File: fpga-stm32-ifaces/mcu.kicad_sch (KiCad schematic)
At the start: 58 parts, among them J10 CORTEX_DEBUG_ETM, J3 PMOD_HOST, J4 XILINX_JTAG, J5 CONN_01X03, U1 STM32H735-UFBGA176-25, U16 W25Q128JV, U2 XC7S25-1FTGB196, U8 AT24MAC402, U9 ECS-1612MV-250-CN

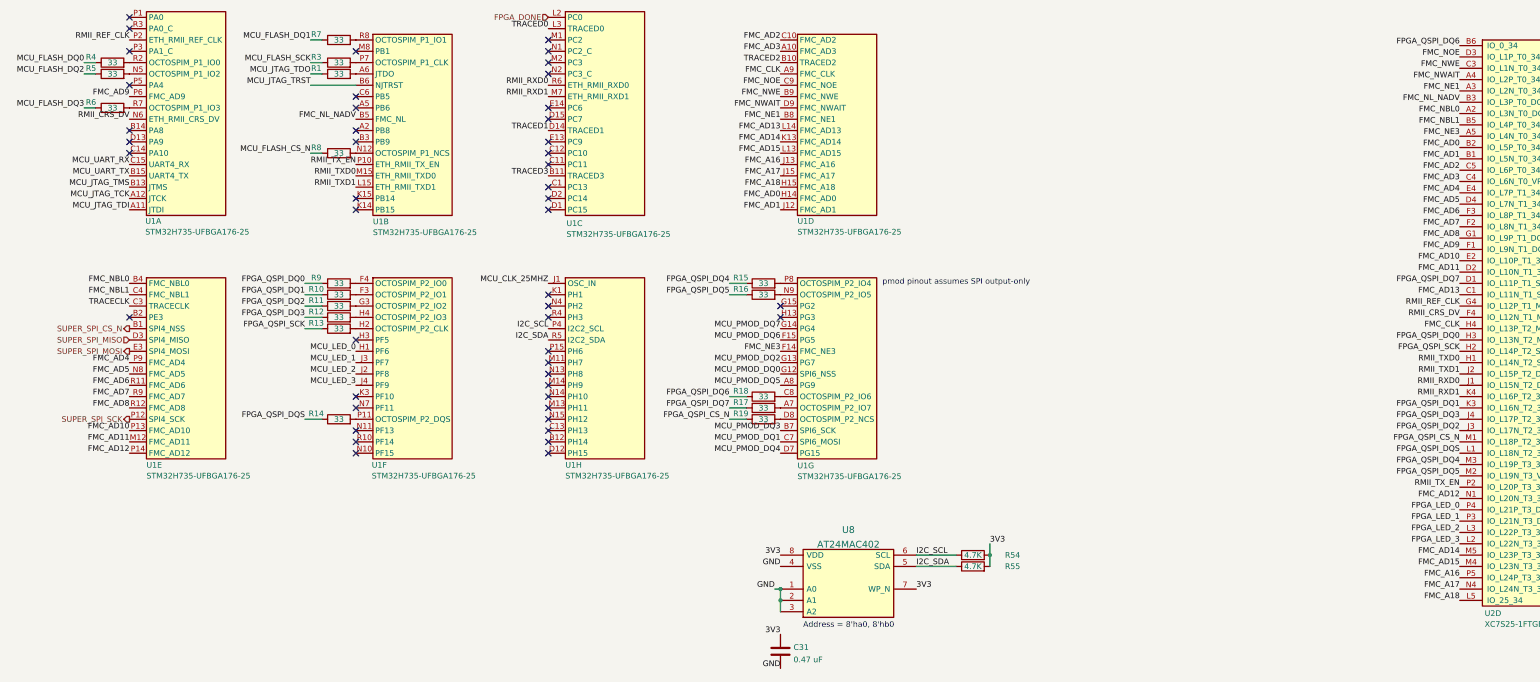
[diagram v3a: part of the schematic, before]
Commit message: Routed most FPGA decoupling caps plus most of RGMII
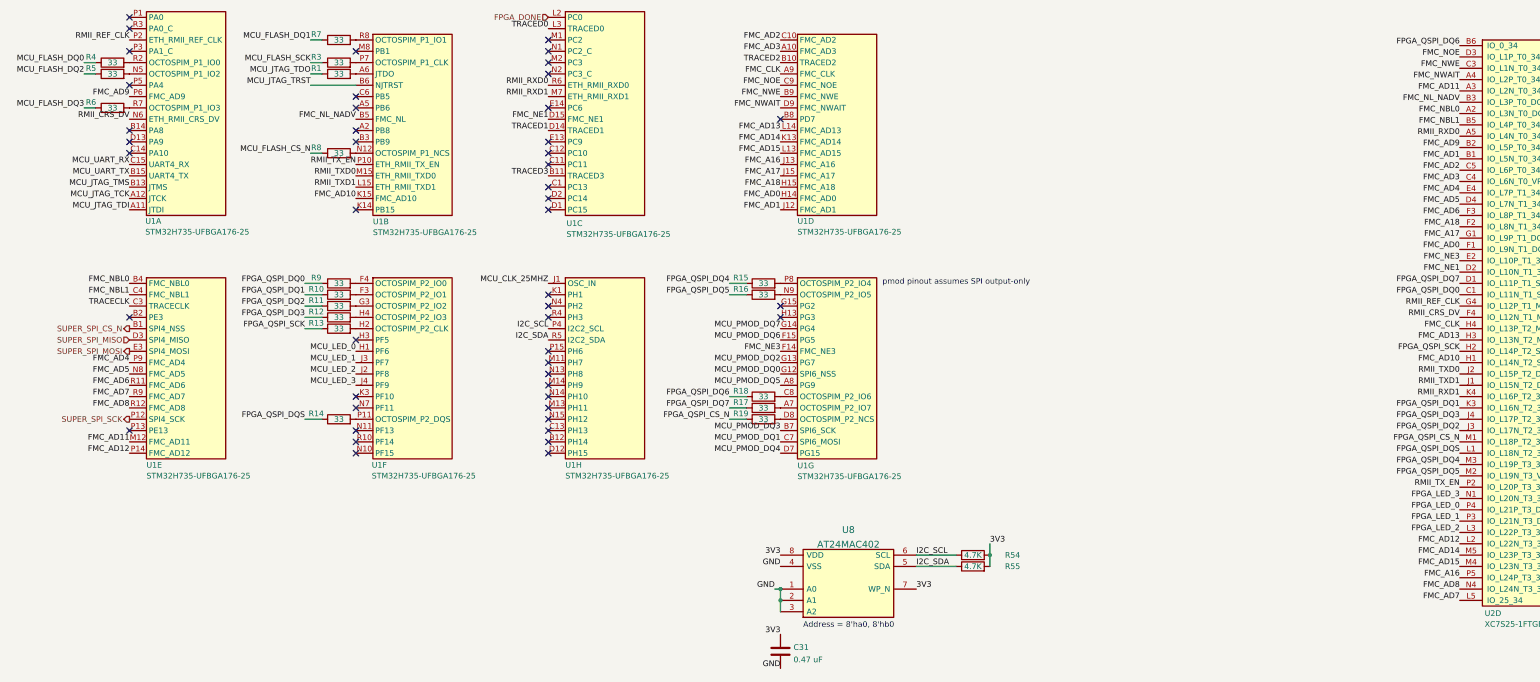
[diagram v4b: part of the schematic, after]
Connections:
- net FMC_A17: now also U2.G1 (IO_L9P_T1_DQS_34); no longer U2.N4 (IO_L24N_T3_34)
- net FMC_A18: now also U2.F2 (IO_L8N_T1_34); no longer U2.L5 (IO_25_34)
- net FMC_AD0: now also U2.F1 (IO_L9N_T1_DQS_34); no longer U2.B2 (IO_L5P_T0_34)
- net FMC_AD10: now also U1.K15 (PB14), U2.H1 (IO_L14N_T2_SRCC_34); no longer U1.P13 (PE13), U2.E2 (IO_L10P_T1_34)
- net FMC_AD11: now also U2.A3 (IO_L2N_T0_34); no longer U2.D2 (IO_L10N_T1_34)
- net FMC_AD12: now also U2.L2 (IO_L22N_T3_34); no longer U2.N1 (IO_L20N_T3_34)
- net FMC_AD13: now also U2.H3 (IO_L13N_T2_MRCC_34); no longer U2.C1 (IO_L11N_T1_SRCC_34)
- net FMC_AD7: now also U2.L5 (IO_25_34); no longer U2.F2 (IO_L8N_T1_34)
- net FMC_AD8: now also U2.N4 (IO_L24N_T3_34); no longer U2.G1 (IO_L9P_T1_DQS_34)
- net FMC_AD9: now also U2.B2 (IO_L5P_T0_34); no longer U2.F1 (IO_L9N_T1_DQS_34)
- net FMC_NE1: now also U1.D15 (PC7), U2.D2 (IO_L10N_T1_34); no longer U1.B8 (PD7), U2.A3 (IO_L2N_T0_34)
- net FMC_NE3: now also U2.E2 (IO_L10P_T1_34); no longer U2.A5 (IO_L4N_T0_34)
- net FPGA_LED_3: now also U2.N1 (IO_L20N_T3_34); no longer U2.L2 (IO_L22N_T3_34)
- net FPGA_QSPI_DQ0: now also U2.C1 (IO_L11N_T1_SRCC_34); no longer U2.H3 (IO_L13N_T2_MRCC_34)
- net RMII_RXD0: now also U2.A5 (IO_L4N_T0_34); no longer U2.J1 (IO_L15N_T2_DQS_34)
- net RMII_TXD0: now also U2.J2 (IO_L15P_T2_DQS_34); no longer U2.H1 (IO_L14N_T2_SRCC_34)
- net RMII_TXD1: now also U2.J1 (IO_L15N_T2_DQS_34); no longer U2.J2 (IO_L15P_T2_DQS_34)
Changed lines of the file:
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@@
 	)
 	(no_connect
+		(at 186.69 53.34)
+	)
+	(no_connect
 		(at 134.62 40.64)
 	)
@@
 	)
 	(no_connect
+		(at 40.64 123.19)
+	)
+	(no_connect
 		(at 134.62 125.73)
 	)
@@
 	)
 	(no_connect
-		(at 134.62 53.34)
-	)
-	(no_connect
 		(at 40.64 58.42)
 	)
@@
 	)
 	(no_connect
-		(at 91.44 71.12)
-	)
-	(no_connect
 		(at 134.62 107.95)
 	)
@@
 	)
 	(label "FMC_AD10"
-		(at 339.09 85.09 180)
+		(at 339.09 107.95 180)
 		(fields_autoplaced yes)
 		(effects
@@
 	)
 	(label "RMII_RXD0"
-		(at 339.09 113.03 180)
+		(at 339.09 57.15 180)
 		(fields_autoplaced yes)
 		(effects
@@
 	)
 	(label "FPGA_QSPI_DQ0"
-		(at 339.09 102.87 180)
+		(at 339.09 92.71 180)
 		(fields_autoplaced yes)
 		(effects
@@
 	)
 	(label "FMC_AD9"
-		(at 339.09 82.55 180)
+		(at 339.09 59.69 180)
 		(fields_autoplaced yes)
 		(effects
@@
 	)
 	(label "FMC_NE1"
-		(at 339.09 46.99 180)
+		(at 339.09 87.63 180)
 		(fields_autoplaced yes)
 		(effects
@@
 	)
 	(label "RMII_TXD1"
-		(at 339.09 110.49 180)
+		(at 339.09 113.03 180)
 		(fields_autoplaced yes)
 		(effects
@@
 	)
 	(label "FMC_AD11"
-		(at 339.09 87.63 180)
+		(at 339.09 46.99 180)
 		(fields_autoplaced yes)
 		(effects
@@
 	)
 	(label "FMC_AD13"
-		(at 339.09 92.71 180)
+		(at 339.09 102.87 180)
 		(fields_autoplaced yes)
 		(effects
@@
 	)
 	(label "FMC_NE1"
-		(at 186.69 53.34 180)
+		(at 134.62 53.34 180)
 		(fields_autoplaced yes)
 		(effects
@@
 	)
 	(label "FMC_AD7"
-		(at 339.09 77.47 180)
+		(at 339.09 161.29 180)
 		(fields_autoplaced yes)
 		(effects
@@
 	)
 	(label "FMC_AD0"
-		(at 339.09 59.69 180)
+		(at 339.09 82.55 180)
 		(fields_autoplaced yes)
 		(effects
@@
 	)
 	(label "FMC_NE3"
-		(at 339.09 57.15 180)
+		(at 339.09 85.09 180)
 		(fields_autoplaced yes)
 		(effects
@@
 	)
 	(label "FMC_AD12"
-		(at 339.09 138.43 180)
+		(at 339.09 148.59 180)
 		(fields_autoplaced yes)
 		(effects
@@
 	)
 	(label "FPGA_LED_3"
-		(at 339.09 148.59 180)
+		(at 339.09 138.43 180)
 		(fields_autoplaced yes)
 		(effects
@@
 	)
 	(label "FMC_A18"
-		(at 339.09 161.29 180)
+		(at 339.09 77.47 180)
 		(fields_autoplaced yes)
 		(effects
@@
 	)
 	(label "FMC_A17"
-		(at 339.09 158.75 180)
+		(at 339.09 80.01 180)
 		(fields_autoplaced yes)
 		(effects
@@
 	)
 	(label "FMC_AD8"
-		(at 339.09 80.01 180)
+		(at 339.09 158.75 180)
 		(fields_autoplaced yes)
 		(effects
@@
 	)
 	(label "RMII_TXD0"
-		(at 339.09 107.95 180)
+		(at 339.09 110.49 180)
 		(fields_autoplaced yes)
 		(effects
@@
 	)
 	(label "FMC_AD10"
-		(at 40.64 123.19 180)
+		(at 91.44 71.12 180)
 		(fields_autoplaced yes)
 		(effects
@@
 		)
 		(pin "B8"
-			(alternate "FMC_NE1")
 		)
 		(pin "D13"
@@
 		)
 		(pin "P13"
-			(alternate "FMC_AD10")
 		)
 		(pin "D14"
@@
 		)
 		(pin "D15"
+			(alternate "FMC_NE1")
 		)
 		(pin "N14"
@@
 		)
 		(pin "K15"
+			(alternate "FMC_AD10")
 		)
 		(pin "P14"
@@
 		)
 		(pin "B8"
-			(alternate "FMC_NE1")
 		)
 		(pin "D13"
@@
 		)
 		(pin "P13"
-			(alternate "FMC_AD10")
 		)
 		(pin "D14"
@@
 		)
 		(pin "D15"
+			(alternate "FMC_NE1")
 		)
 		(pin "N14"
@@
 		)
 		(pin "K15"
+			(alternate "FMC_AD10")
 		)
 		(pin "P14"
@@
 		)
 		(pin "B8"
-			(alternate "FMC_NE1")
 		)
 		(pin "D13"
@@
 		)
 		(pin "P13"
-			(alternate "FMC_AD10")
 		)
 		(pin "D14"
@@
 		)
 		(pin "D15"
+			(alternate "FMC_NE1")
 		)
 		(pin "N14"
@@
 		)
 		(pin "K15"
+			(alternate "FMC_AD10")
 		)
 		(pin "P14"
@@
 		)
 		(pin "B8"
-			(alternate "FMC_NE1")
 		)
 		(pin "D13"
@@
 		)
 		(pin "P13"
-			(alternate "FMC_AD10")
 		)
 		(pin "D14"
@@
 		)
 		(pin "D15"
+			(alternate "FMC_NE1")
 		)
 		(pin "N14"
@@
 		)
 		(pin "K15"
+			(alternate "FMC_AD10")
 		)
 		(pin "P14"
@@
 		)
 		(pin "B8"
-			(alternate "FMC_NE1")
 		)
 		(pin "D13"
@@
 		)
 		(pin "P13"
-			(alternate "FMC_AD10")
 		)
 		(pin "D14"
@@
 		)
 		(pin "D15"
+			(alternate "FMC_NE1")
 		)
 		(pin "N14"
@@
 		)
 		(pin "K15"
+			(alternate "FMC_AD10")
 		)
 		(pin "P14"
@@
 		)
 		(pin "B8"
-			(alternate "FMC_NE1")
 		)
 		(pin "D13"
@@
 		)
 		(pin "P13"
-			(alternate "FMC_AD10")
 		)
 		(pin "D14"
@@
 		)
 		(pin "D15"
+			(alternate "FMC_NE1")
 		)
 		(pin "N14"
@@
 		)
 		(pin "K15"
+			(alternate "FMC_AD10")
 		)
 		(pin "P14"
@@
 		)
 		(pin "B8"
-			(alternate "FMC_NE1")
 		)
 		(pin "D13"
@@
 		)
 		(pin "P13"
-			(alternate "FMC_AD10")
 		)
 		(pin "D14"
@@
 		)
 		(pin "D15"
+			(alternate "FMC_NE1")
 		)
 		(pin "N14"
@@
 		)
 		(pin "K15"
+			(alternate "FMC_AD10")
 		)
 		(pin "P14"
@@
 		)
 		(pin "B8"
-			(alternate "FMC_NE1")
 		)
 		(pin "D13"
@@
 		)
 		(pin "P13"
-			(alternate "FMC_AD10")
 		)
 		(pin "D14"
@@
 		)
 		(pin "D15"
+			(alternate "FMC_NE1")
 		)
 		(pin "N14"
@@
 		)
 		(pin "K15"
+			(alternate "FMC_AD10")
 		)
 		(pin "P14"

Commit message: Continued layout, 283 now unrouted
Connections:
- net FMC_AD11: now also U2.L1 (IO_L18N_T2_34); no longer U2.A3 (IO_L2N_T0_34)
- net FMC_AD3: now also U2.D1 (IO_L11P_T1_SRCC_34); no longer U2.C4 (IO_L6N_T0_VREF_34)
- net FMC_AD4: now also U2.P2 (IO_L20P_T3_34); no longer U2.E4 (IO_L7P_T1_34)
- net FMC_AD6: now also U2.M2 (IO_L19N_T3_VREF_34); no longer U2.F3 (IO_L8P_T1_34)
- net FMC_AD8: now also U2.M1 (IO_L18P_T2_34); no longer U2.N4 (IO_L24N_T3_34)
- net FMC_NWAIT: now also U1.E14 (PC6); no longer U1.D9 (PD6)
- net FPGA_LED_3: now also U2.E4 (IO_L7P_T1_34); no longer U2.N1 (IO_L20N_T3_34)
- net FPGA_QSPI_CS_N: now also U2.N4 (IO_L24N_T3_34); no longer U2.M1 (IO_L18P_T2_34)
- net FPGA_QSPI_DQ5: now also U2.F3 (IO_L8P_T1_34); no longer U2.M2 (IO_L19N_T3_VREF_34)
- net FPGA_QSPI_DQ7: now also U2.C4 (IO_L6N_T0_VREF_34); no longer U2.D1 (IO_L11P_T1_SRCC_34)
- net FPGA_QSPI_DQS: now also U2.A3 (IO_L2N_T0_34); no longer U2.L1 (IO_L18N_T2_34)
- net MCU_PMOD_DQ2: now also U1.D7 (PG15); no longer U1.G13 (PG7)
- net MCU_PMOD_DQ4: now also U1.G13 (PG7); no longer U1.D7 (PG15)
- net MCU_PMOD_DQ5: now also U1.G14 (PG4); no longer U1.A8 (PG9)
- net MCU_PMOD_DQ7: now also U1.A8 (PG9); no longer U1.G14 (PG4)
- net RMII_TX_EN: now also U2.N1 (IO_L20N_T3_34); no longer U2.P2 (IO_L20P_T3_34)
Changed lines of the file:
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@@
 	(title_block
 		(title "FPGA - STM32 Interface Test")
-		(date "2024-06-12")
+		(date "2024-06-13")
 		(rev "0.1")
 		(company "Antikernel Labs")
@@
 	)
 	(no_connect
-		(at 134.62 50.8)
-	)
-	(no_connect
 		(at 91.44 102.87)
 	)
@@
 	)
 	(no_connect
+		(at 186.69 50.8)
+	)
+	(no_connect
 		(at 40.64 60.96)
 	)
@@
 	)
 	(label "MCU_PMOD_DQ4"
-		(at 186.69 128.27 180)
+		(at 186.69 107.95 180)
 		(fields_autoplaced yes)
 		(effects
@@
 	)
 	(label "FPGA_QSPI_DQS"
-		(at 339.09 128.27 180)
+		(at 339.09 46.99 180)
 		(fields_autoplaced yes)
 		(effects
@@
 	)
 	(label "FMC_AD3"
-		(at 339.09 67.31 180)
+		(at 339.09 90.17 180)
 		(fields_autoplaced yes)
 		(effects
@@
 	)
 	(label "MCU_PMOD_DQ7"
-		(at 186.69 100.33 180)
+		(at 186.69 113.03 180)
 		(fields_autoplaced yes)
 		(effects
@@
 	)
 	(label "FMC_AD4"
-		(at 339.09 69.85 180)
+		(at 339.09 135.89 180)
 		(fields_autoplaced yes)
 		(effects
@@
 	)
 	(label "FPGA_QSPI_DQ7"
-		(at 339.09 90.17 180)
+		(at 339.09 67.31 180)
 		(fields_autoplaced yes)
 		(effects
@@
 	)
 	(label "MCU_PMOD_DQ5"
-		(at 186.69 113.03 180)
+		(at 186.69 100.33 180)
 		(fields_autoplaced yes)
 		(effects
@@
 	)
 	(label "FPGA_QSPI_CS_N"
-		(at 339.09 125.73 180)
+		(at 339.09 158.75 180)
 		(fields_autoplaced yes)
 		(effects
@@
 	)
 	(label "RMII_TX_EN"
-		(at 339.09 135.89 180)
+		(at 339.09 138.43 180)
 		(fields_autoplaced yes)
 		(effects
@@
 	)
 	(label "FPGA_QSPI_DQ5"
-		(at 339.09 133.35 180)
+		(at 339.09 74.93 180)
 		(fields_autoplaced yes)
 		(effects
@@
 	)
 	(label "FMC_AD11"
-		(at 339.09 46.99 180)
+		(at 339.09 128.27 180)
 		(fields_autoplaced yes)
 		(effects
@@
 	)
 	(label "MCU_PMOD_DQ2"
-		(at 186.69 107.95 180)
+		(at 186.69 128.27 180)
 		(fields_autoplaced yes)
 		(effects
@@
 	)
 	(label "FMC_NWAIT"
-		(at 186.69 50.8 180)
+		(at 134.62 50.8 180)
 		(fields_autoplaced yes)
 		(effects
@@
 	)
 	(label "FMC_AD6"
-		(at 339.09 74.93 180)
+		(at 339.09 133.35 180)
 		(fields_autoplaced yes)
 		(effects
@@
 	)
 	(label "FPGA_LED_3"
-		(at 339.09 138.43 180)
+		(at 339.09 69.85 180)
 		(fields_autoplaced yes)
 		(effects
@@
 	)
 	(label "FMC_AD8"
-		(at 339.09 158.75 180)
+		(at 339.09 125.73 180)
 		(fields_autoplaced yes)
 		(effects
@@
 		)
 		(pin "D9"
-			(alternate "FMC_NWAIT")
 		)
 		(pin "M8"
@@
 		)
 		(pin "E14"
+			(alternate "FMC_NWAIT")
 		)
 		(pin "A8"
@@
 		)
 		(pin "D9"
-			(alternate "FMC_NWAIT")
 		)
 		(pin "M8"
@@
 		)
 		(pin "E14"
+			(alternate "FMC_NWAIT")
 		)
 		(pin "A8"
@@
 		)
 		(pin "D9"
-			(alternate "FMC_NWAIT")
 		)
 		(pin "M8"
@@
 		)
 		(pin "E14"
+			(alternate "FMC_NWAIT")
 		)
 		(pin "A8"
@@
 		)
 		(pin "D9"
-			(alternate "FMC_NWAIT")
 		)
 		(pin "M8"
@@
 		)
 		(pin "E14"
+			(alternate "FMC_NWAIT")
 		)
 		(pin "A8"
@@
 		)
 		(pin "D9"
-			(alternate "FMC_NWAIT")
 		)
 		(pin "M8"
@@
 		)
 		(pin "E14"
+			(alternate "FMC_NWAIT")
 		)
 		(pin "A8"
@@
 		)
 		(pin "D9"
-			(alternate "FMC_NWAIT")
 		)
 		(pin "M8"
@@
 		)
 		(pin "E14"
+			(alternate "FMC_NWAIT")
 		)
 		(pin "A8"
@@
 		)
 		(pin "D9"
-			(alternate "FMC_NWAIT")
 		)
 		(pin "M8"
@@
 		)
 		(pin "E14"
+			(alternate "FMC_NWAIT")
 		)
 		(pin "A8"
@@
 		)
 		(pin "D9"
-			(alternate "FMC_NWAIT")
 		)
 		(pin "M8"
@@
 		)
 		(pin "E14"
+			(alternate "FMC_NWAIT")
 		)
 		(pin "A8"

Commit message: Lots more routing around FPGA and MCU
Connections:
- net FMC_A16: now also U2.E4 (IO_L7P_T1_34); no longer U2.P5 (IO_L24P_T3_34)
- net FMC_AD15: now also U2.A5 (IO_L4N_T0_34); no longer U2.M4 (IO_L23N_T3_34)
- net FMC_AD7: now also U2.M3 (IO_L19P_T3_34); no longer U2.L5 (IO_25_34)
- net FPGA_DONE: now also U1.P1 (PA0); no longer U1.L2 (PC0)
- net FPGA_LED_0: now also U2.P3 (IO_L21N_T3_DQS_34); no longer U2.P4 (IO_L21P_T3_DQS_34)
- net FPGA_LED_1: now also U2.N4 (IO_L24N_T3_34); no longer U2.P3 (IO_L21N_T3_DQS_34)
- net FPGA_LED_2: now also U2.P4 (IO_L21P_T3_DQS_34); no longer U2.L3 (IO_L22P_T3_34)
- net FPGA_LED_3: now also U2.P5 (IO_L24P_T3_34); no longer U2.E4 (IO_L7P_T1_34)
- net FPGA_QSPI_CS_N: now also U2.L3 (IO_L22P_T3_34); no longer U2.N4 (IO_L24N_T3_34)
- net FPGA_QSPI_DQ4: now also U2.L5 (IO_25_34); no longer U2.M3 (IO_L19P_T3_34)
- net RMII_RXD0: now also U2.M4 (IO_L23N_T3_34); no longer U2.A5 (IO_L4N_T0_34)
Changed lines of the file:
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@@
-	)
-	(no_connect
-		(at 40.64 30.48)
 	)
 	(no_connect
@@
 	(no_connect
 		(at 40.64 123.19)
+	)
+	(no_connect
+		(at 134.62 30.48)
 	)
 	(no_connect
@@
 	)
 	(label "FPGA_LED_1"
-		(at 339.09 143.51 180)
+		(at 339.09 158.75 180)
 		(fields_autoplaced yes)
 		(effects
@@
 	)
 	(label "FPGA_LED_2"
-		(at 339.09 146.05 180)
+		(at 339.09 140.97 180)
 		(fields_autoplaced yes)
 		(effects
@@
 	)
 	(label "RMII_RXD0"
-		(at 339.09 57.15 180)
+		(at 339.09 153.67 180)
 		(fields_autoplaced yes)
 		(effects
@@
 	)
 	(label "FPGA_QSPI_CS_N"
-		(at 339.09 158.75 180)
+		(at 339.09 146.05 180)
 		(fields_autoplaced yes)
 		(effects
@@
 	)
 	(label "FPGA_QSPI_DQ4"
-		(at 339.09 130.81 180)
+		(at 339.09 161.29 180)
 		(fields_autoplaced yes)
 		(effects
@@
 	)
 	(label "FMC_A16"
-		(at 339.09 156.21 180)
+		(at 339.09 69.85 180)
 		(fields_autoplaced yes)
 		(effects
@@
 	)
 	(label "FMC_AD7"
-		(at 339.09 161.29 180)
+		(at 339.09 130.81 180)
 		(fields_autoplaced yes)
 		(effects
@@
 	)
 	(label "FMC_AD15"
-		(at 339.09 153.67 180)
+		(at 339.09 57.15 180)
 		(fields_autoplaced yes)
 		(effects
@@
 	)
 	(label "FPGA_LED_3"
-		(at 339.09 69.85 180)
+		(at 339.09 156.21 180)
 		(fields_autoplaced yes)
 		(effects
@@
 	)
 	(label "FPGA_LED_0"
-		(at 339.09 140.97 180)
+		(at 339.09 143.51 180)
 		(fields_autoplaced yes)
 		(effects
@@
 	(hierarchical_label "FPGA_DONE"
 		(shape input)
-		(at 134.62 30.48 180)
-		(fields_autoplaced yes)
-		(effects
+		(at 40.64 30.48 180)
+		(fields_autoplaced yes)
+		(effects

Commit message: Continued fpga-stm32-ifaces layout
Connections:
- net FMC_AD1: now also U2.D4 (IO_L7N_T1_34); no longer U2.B1 (IO_L5N_T0_34)
- net FMC_AD14: now also U2.F3 (IO_L8P_T1_34); no longer U2.M5 (IO_L23P_T3_34)
- net FMC_AD15: now also U2.F4 (IO_L12N_T1_MRCC_34); no longer U2.A5 (IO_L4N_T0_34)
- net FMC_AD2: now also U2.D3 (IO_L1P_T0_34); no longer U2.C5 (IO_L6P_T0_34)
- net FMC_AD5: now also U2.J3 (IO_L17N_T2_34); no longer U2.D4 (IO_L7N_T1_34)
- net FMC_AD9: now also U2.K3 (IO_L16N_T2_34); no longer U2.B2 (IO_L5P_T0_34)
- net FMC_NBL0: now also U2.B1 (IO_L5N_T0_34); no longer U2.A2 (IO_L3N_T0_DQS_34)
- net FMC_NL_NADV: now also U2.C1 (IO_L11N_T1_SRCC_34); no longer U2.B3 (IO_L3P_T0_DQS_34)
- net FMC_NOE: now also U2.A4 (IO_L2P_T0_34); no longer U2.D3 (IO_L1P_T0_34)
- net FMC_NWAIT: now also U2.C3 (IO_L1N_T0_34); no longer U2.A4 (IO_L2P_T0_34)
- net FMC_NWE: now also U2.A2 (IO_L3N_T0_DQS_34); no longer U2.C3 (IO_L1N_T0_34)
- net FPGA_QSPI_CS_N: now also U2.A3 (IO_L2N_T0_34); no longer U2.L3 (IO_L22P_T3_34)
- net FPGA_QSPI_DQ0: now also U2.B3 (IO_L3P_T0_DQS_34); no longer U2.C1 (IO_L11N_T1_SRCC_34)
- net FPGA_QSPI_DQ1: now also U2.C4 (IO_L6N_T0_VREF_34); no longer U2.K3 (IO_L16N_T2_34)
- net FPGA_QSPI_DQ2: now also U2.C5 (IO_L6P_T0_34); no longer U2.J3 (IO_L17N_T2_34)
- net FPGA_QSPI_DQ3: now also U2.B6 (IO_0_34); no longer U2.J4 (IO_L17P_T2_34)
- net FPGA_QSPI_DQ4: now also U2.M5 (IO_L23P_T3_34); no longer U2.L5 (IO_25_34)
- net FPGA_QSPI_DQ5: now also U2.L5 (IO_25_34); no longer U2.F3 (IO_L8P_T1_34)
- net FPGA_QSPI_DQ6: now also U2.A5 (IO_L4N_T0_34); no longer U2.B6 (IO_0_34)
- net FPGA_QSPI_DQ7: now also U2.B2 (IO_L5P_T0_34); no longer U2.C4 (IO_L6N_T0_VREF_34)
- net FPGA_QSPI_DQS: now also U2.L3 (IO_L22P_T3_34); no longer U2.A3 (IO_L2N_T0_34)
- net RMII_CRS_DV: now also U2.K4 (IO_L16P_T2_34); no longer U2.F4 (IO_L12N_T1_MRCC_34)
- net RMII_RXD1: now also U2.J4 (IO_L17P_T2_34); no longer U2.K4 (IO_L16P_T2_34)
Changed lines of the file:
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@@
 	)
 	(label "FMC_NWAIT"
-		(at 339.09 44.45 180)
+		(at 339.09 41.91 180)
 		(fields_autoplaced yes)
 		(effects
@@
 	)
 	(label "FPGA_QSPI_DQS"
-		(at 339.09 46.99 180)
+		(at 339.09 146.05 180)
 		(fields_autoplaced yes)
 		(effects
@@
 	)
 	(label "FMC_NOE"
-		(at 339.09 39.37 180)
+		(at 339.09 44.45 180)
 		(fields_autoplaced yes)
 		(effects
@@
 	)
 	(label "RMII_RXD1"
-		(at 339.09 115.57 180)
+		(at 339.09 120.65 180)
 		(fields_autoplaced yes)
 		(effects
@@
 	)
 	(label "FPGA_QSPI_DQ0"
-		(at 339.09 92.71 180)
+		(at 339.09 49.53 180)
 		(fields_autoplaced yes)
 		(effects
@@
 	)
 	(label "FMC_AD9"
-		(at 339.09 59.69 180)
+		(at 339.09 118.11 180)
 		(fields_autoplaced yes)
 		(effects
@@
 	)
 	(label "FPGA_QSPI_DQ7"
-		(at 339.09 67.31 180)
+		(at 339.09 59.69 180)
 		(fields_autoplaced yes)
 		(effects
@@
 	)
 	(label "FMC_AD14"
-		(at 339.09 151.13 180)
+		(at 339.09 74.93 180)
 		(fields_autoplaced yes)
 		(effects
@@
 	)
 	(label "FPGA_QSPI_CS_N"
-		(at 339.09 146.05 180)
+		(at 339.09 46.99 180)
 		(fields_autoplaced yes)
 		(effects
@@
 	)
 	(label "FPGA_QSPI_DQ4"
-		(at 339.09 161.29 180)
+		(at 339.09 151.13 180)
 		(fields_autoplaced yes)
 		(effects
@@
 	)
 	(label "FMC_AD5"
-		(at 339.09 72.39 180)
+		(at 339.09 123.19 180)
 		(fields_autoplaced yes)
 		(effects
@@
 	)
 	(label "RMII_CRS_DV"
-		(at 339.09 97.79 180)
+		(at 339.09 115.57 180)
 		(fields_autoplaced yes)
 		(effects
@@
 	)
 	(label "FPGA_QSPI_DQ1"
-		(at 339.09 118.11 180)
+		(at 339.09 67.31 180)
 		(fields_autoplaced yes)
 		(effects
@@
 	)
 	(label "FPGA_QSPI_DQ5"
-		(at 339.09 74.93 180)
+		(at 339.09 161.29 180)
 		(fields_autoplaced yes)
 		(effects
@@
 	)
 	(label "FMC_NBL0"
-		(at 339.09 52.07 180)
+		(at 339.09 62.23 180)
 		(fields_autoplaced yes)
 		(effects
@@
 	)
 	(label "FPGA_QSPI_DQ2"
-		(at 339.09 123.19 180)
+		(at 339.09 64.77 180)
 		(fields_autoplaced yes)
 		(effects
@@
 	)
 	(label "FMC_AD15"
-		(at 339.09 57.15 180)
+		(at 339.09 97.79 180)
 		(fields_autoplaced yes)
 		(effects
@@
 	)
 	(label "FMC_AD2"
-		(at 339.09 64.77 180)
+		(at 339.09 39.37 180)
 		(fields_autoplaced yes)
 		(effects
@@
 	)
 	(label "FPGA_QSPI_DQ3"
-		(at 339.09 120.65 180)
+		(at 339.09 36.83 180)
 		(fields_autoplaced yes)
 		(effects
@@
 	)
 	(label "FPGA_QSPI_DQ6"
-		(at 339.09 36.83 180)
+		(at 339.09 57.15 180)
 		(fields_autoplaced yes)
 		(effects
@@
 	)
 	(label "FMC_NL_NADV"
-		(at 339.09 49.53 180)
+		(at 339.09 92.71 180)
 		(fields_autoplaced yes)
 		(effects
@@
 	)
 	(label "FMC_NWE"
-		(at 339.09 41.91 180)
+		(at 339.09 52.07 180)
 		(fields_autoplaced yes)
 		(effects
@@
 	)
 	(label "FMC_AD1"
-		(at 339.09 62.23 180)
-		(fields_autoplaced yes)
-		(effects
+		(at 339.09 72.39 180)
+		(fields_autoplaced yes)
+		(effects
